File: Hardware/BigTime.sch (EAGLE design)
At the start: 13 parts, among them U1 ATMEGA328P_PDIP_EZ, Y1 32.768kHz

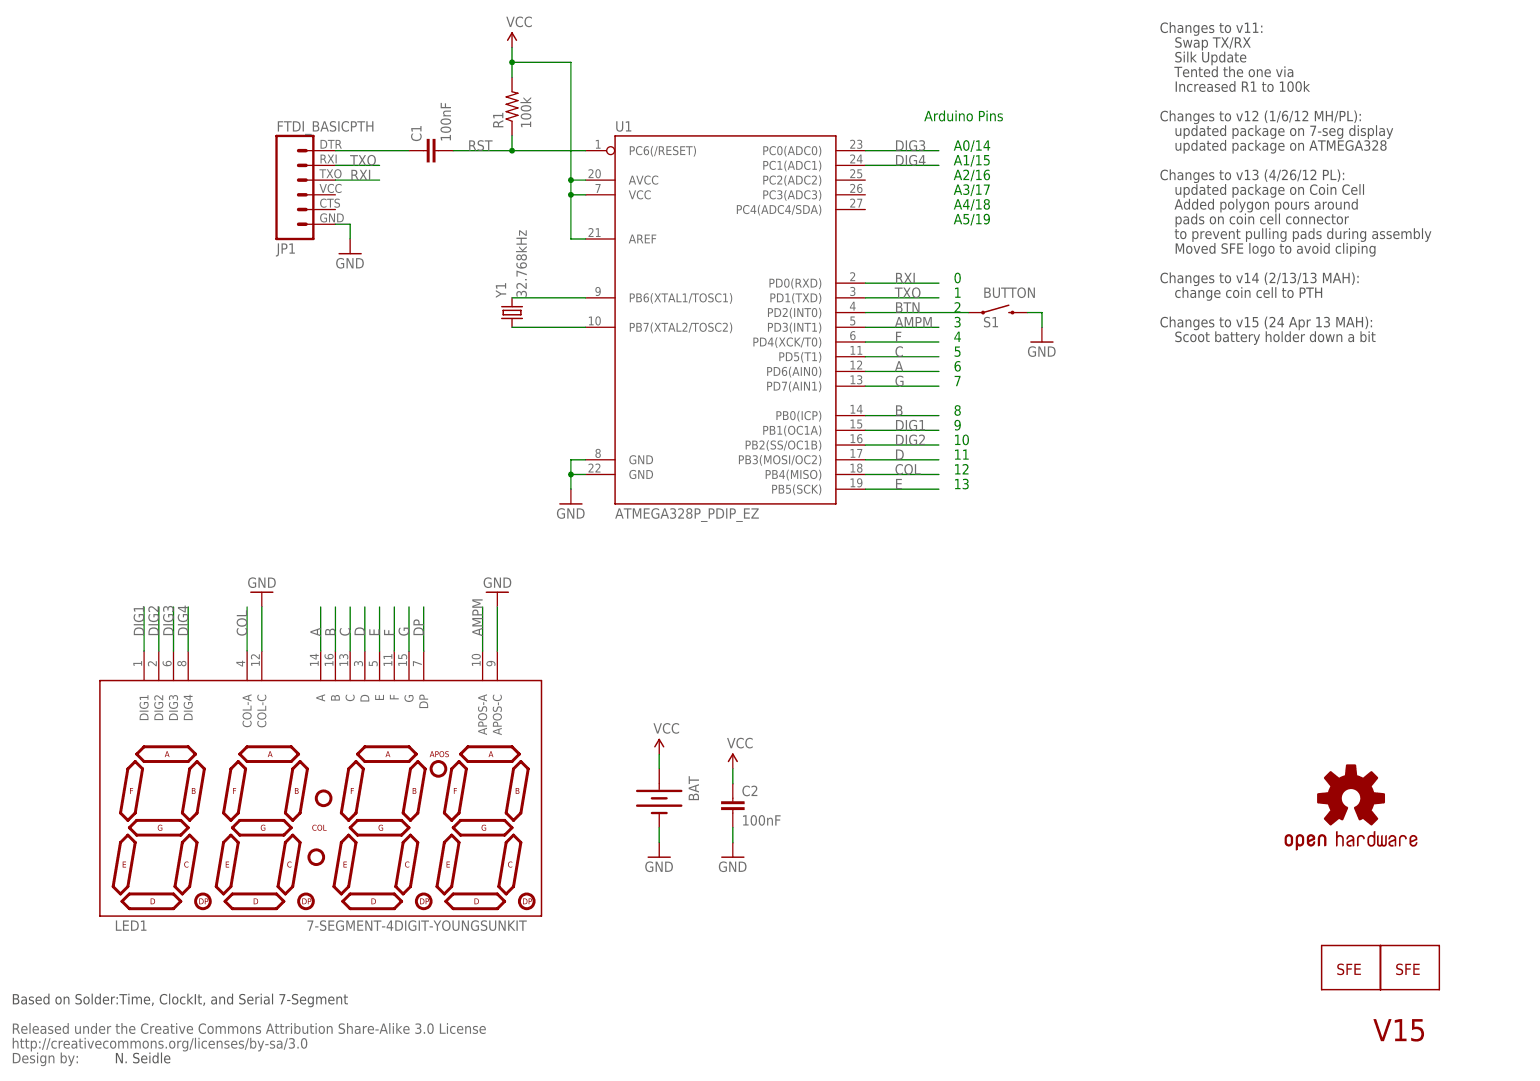
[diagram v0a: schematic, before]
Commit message: replace LED with bubble display
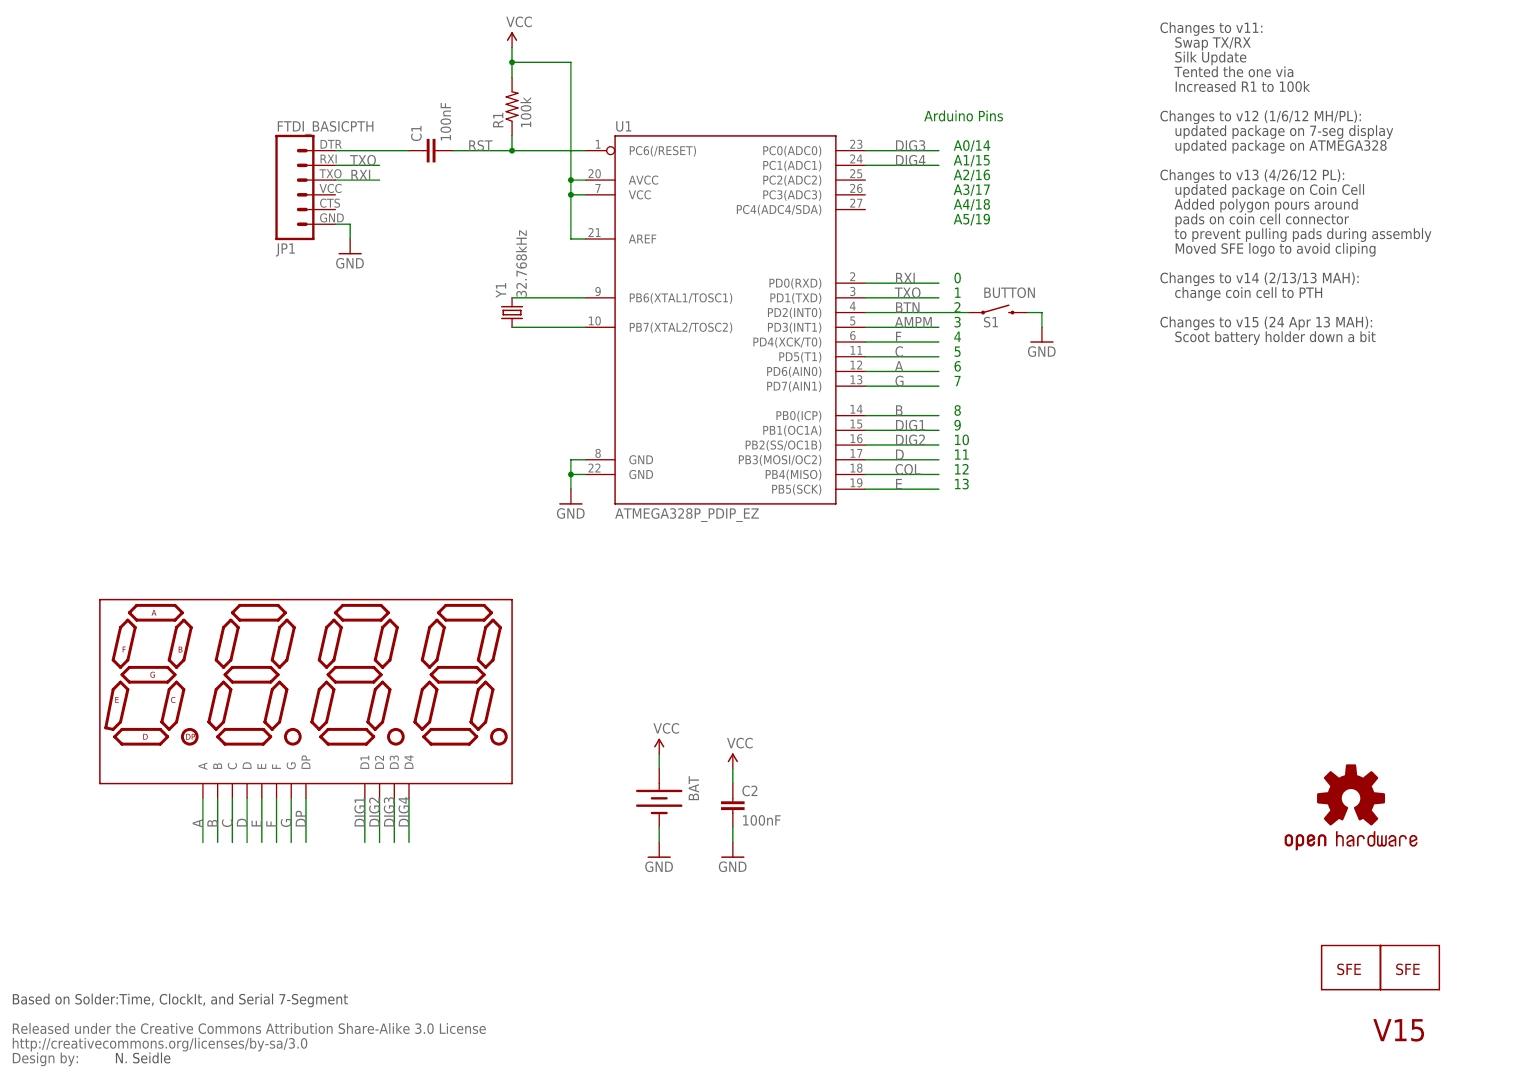
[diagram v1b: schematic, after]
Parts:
- removed LED1: 7-SEGMENT-4DIGIT-YOUNGSUNKIT, Testing:7-SEGMENT-4DIGIT-YOUNGSUNKIT
- added DISP1: 7-SEGMENT-4DIGIT-COUNTER-HP-BUBBLE, SparkFun-Displays:7-SEGMENT-4DIGIT-COUNTER-HP-BUBBLE
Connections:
- net A: now also DISP1.A; no longer LED1.A
- net AMPM: no longer LED1.APOS-A
- net B: now also DISP1.B; no longer LED1.B
- net C: now also DISP1.C; no longer LED1.C
- net COL: no longer LED1.COL-A
- net D: now also DISP1.D; no longer LED1.D
- net DIG1: now also DISP1.D1; no longer LED1.DIG1
- net DIG2: now also DISP1.D2; no longer LED1.DIG2
- net DIG3: now also DISP1.D3; no longer LED1.DIG3
- net DIG4: now also DISP1.D4; no longer LED1.DIG4
- net DP: now also DISP1.DP; no longer LED1.DP
- net E: now also DISP1.E; no longer LED1.E
- net F: now also DISP1.F; no longer LED1.F
- net G: now also DISP1.G; no longer LED1.G
- net GND: no longer LED1.APOS-C, LED1.COL-C

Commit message: add set button, reroute pub
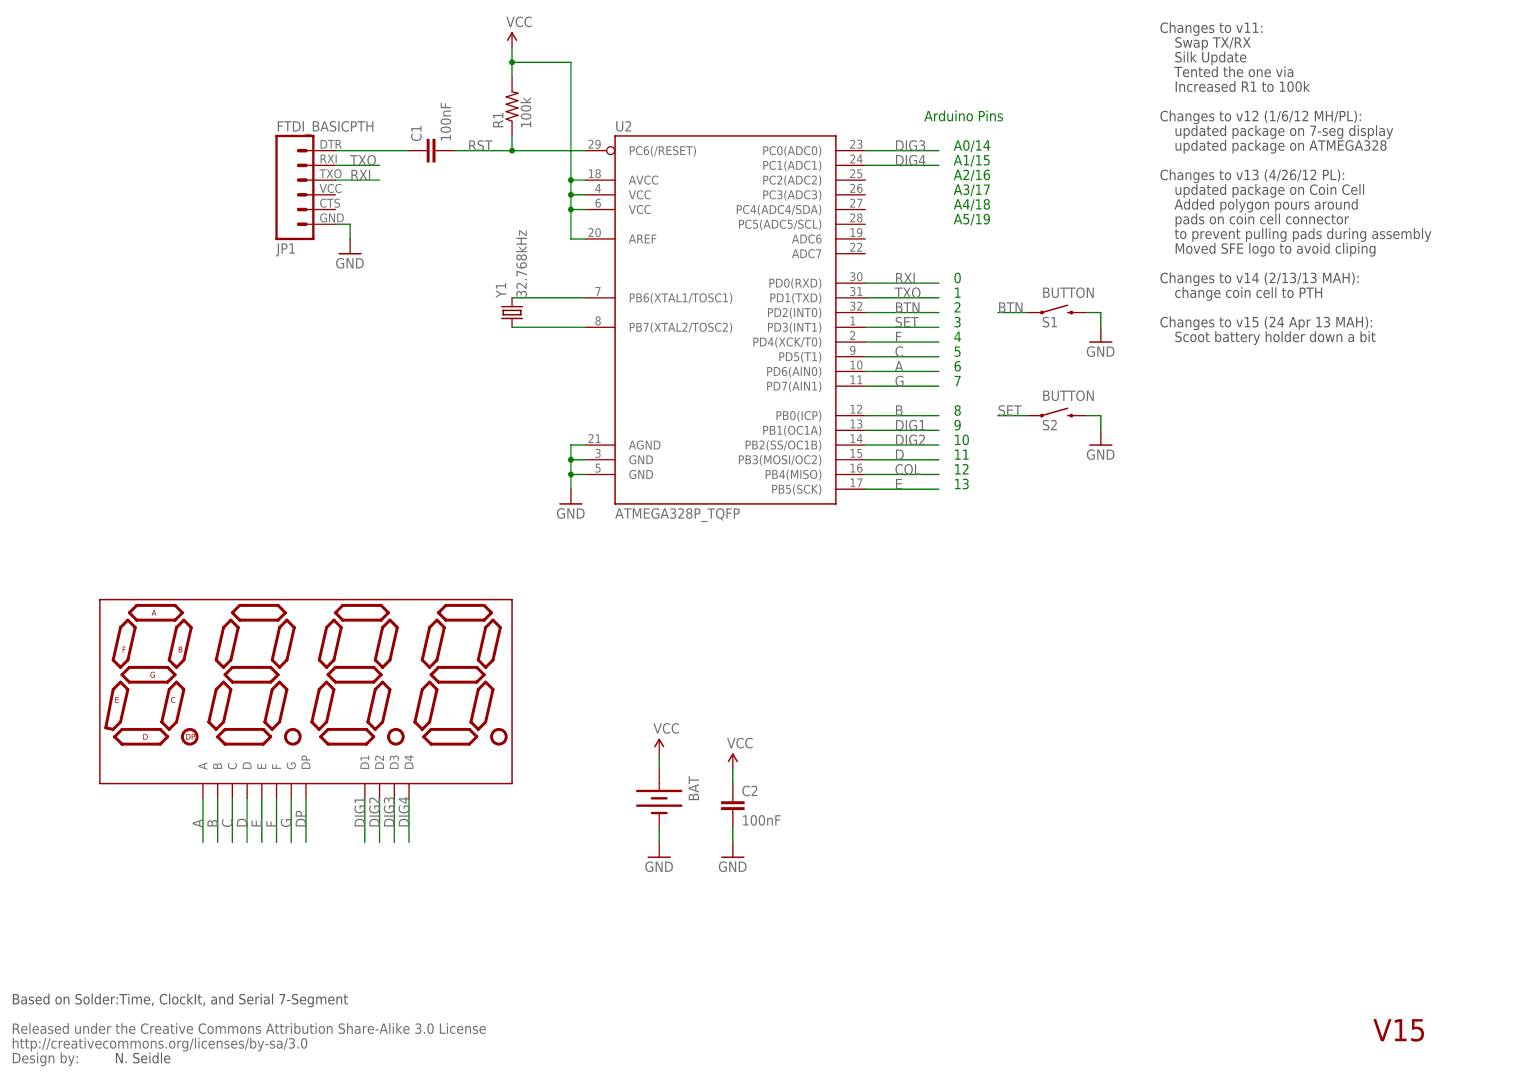
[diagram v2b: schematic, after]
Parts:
- removed U$1: LOGO-SFESK, SparkFun:LOGO-SFESK
- removed U$4: OSHW-LOGOS, SparkFun:OSHW-LOGOS
- removed U$5: LOGO-SFENW2, SparkFun:LOGO-SFENW2
- removed U1: ATMEGA328P_PDIP_EZ, SparkFun-DigitalIC:ATMEGA328P_PDIP_EZ
- added S2: BUTTON, SparkFun-Electromechanical:SWITCH-MOMENTARY-2SIDE_EZ
- added U2: ATMEGA328P_TQFP, SparkFun-DigitalIC:ATMEGA328P_TQFP
- C1, C2: device SparkFun-Passives:CAPEZ -> SparkFun-Passives:CAP0402-CAP
- DISP1: value 7-SEGMENT-4DIGIT-COUNTER-HP-BUBBLE -> 7-SEGMENT-4DIGIT-COUNTER-HP-BUBBLE-SM; device SparkFun-Displays:7-SEGMENT-4DIGIT-COUNTER-HP-BUBBLE -> SparkFun-Displays:7-SEGMENT-4DIGIT-COUNTER-HP-BUBBLE-SM
- R1: device SparkFun-Passives:RESISTORKIT -> SparkFun-Passives:RESISTOR0402-RES
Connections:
- removed net AMPM: U1.PD3(INT1)
- new net SET: S2.1, U2.PD3(INT1)
- net A: now also U2.PD6(AIN0); no longer U1.PD6(AIN0)
- net B: now also U2.PB0(ICP); no longer U1.PB0(ICP)
- net BTN: now also U2.PD2(INT0); no longer U1.PD2(INT0)
- net C: now also U2.PD5(T1); no longer U1.PD5(T1)
- net COL: now also U2.PB4(MISO); no longer U1.PB4(MISO)
- net D: now also U2.PB3(MOSI/OC2); no longer U1.PB3(MOSI/OC2)
- net DIG1: now also U2.PB1(OC1A); no longer U1.PB1(OC1A)
- net DIG2: now also U2.PB2(SS/OC1B); no longer U1.PB2(SS/OC1B)
- net DIG3: now also U2.PC0(ADC0); no longer U1.PC0(ADC0)
- net DIG4: now also U2.PC1(ADC1); no longer U1.PC1(ADC1)
- net E: now also U2.PB5(SCK); no longer U1.PB5(SCK)
- net F: now also U2.PD4(XCK/T0); no longer U1.PD4(XCK/T0)
- net G: now also U2.PD7(AIN1); no longer U1.PD7(AIN1)
- net GND: now also S2.2, U2.AGND, U2.GND@3, U2.GND@5; no longer U1.GND@1, U1.GND@2
- net N$1: now also U2.PB7(XTAL2/TOSC2); no longer U1.PB7(XTAL2/TOSC2)
- net N$2: now also U2.PB6(XTAL1/TOSC1); no longer U1.PB6(XTAL1/TOSC1)
- net RST: now also U2.PC6(/RESET); no longer U1.PC6(/RESET)
- net RXI: now also U2.PD0(RXD); no longer U1.PD0(RXD)
- net TXO: now also U2.PD1(TXD); no longer U1.PD1(TXD)
- net VCC: now also U2.AREF, U2.AVCC, U2.VCC@4, U2.VCC@6; no longer U1.AREF, U1.AVCC, U1.VCC
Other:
- moved on the sheet: S1

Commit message: more efficient pin arrangement
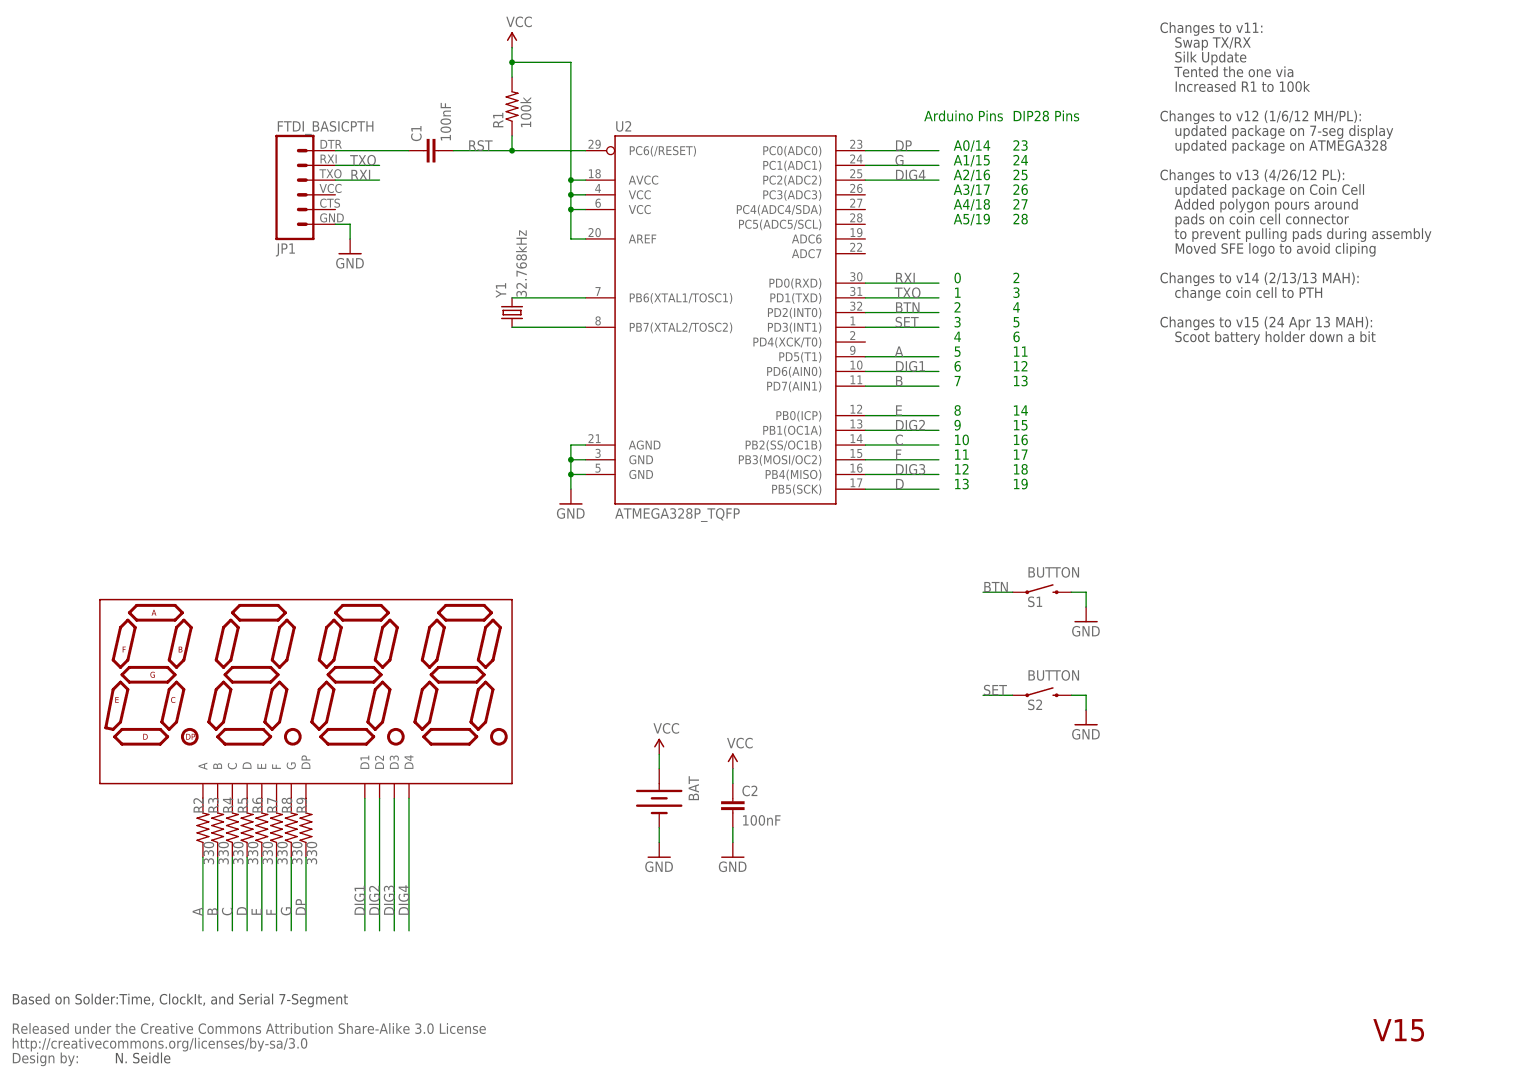
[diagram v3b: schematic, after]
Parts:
- added R2, R3, R4, R5, R6, R7, R8, R9: 330, SparkFun-Passives:RESISTOR0402-RES
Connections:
- removed net COL: U2.PB4(MISO)
- new net N$10: DISP1.G, R8.2
- new net N$11: DISP1.DP, R9.2
- new net N$4: DISP1.A, R2.2
- new net N$5: DISP1.B, R3.2
- new net N$6: DISP1.C, R4.2
- new net N$7: DISP1.D, R5.2
- new net N$8: DISP1.E, R6.2
- new net N$9: DISP1.F, R7.2
- net A: now also R2.1, U2.PD5(T1); no longer DISP1.A, U2.PD6(AIN0)
- net B: now also R3.1, U2.PD7(AIN1); no longer DISP1.B, U2.PB0(ICP)
- net C: now also R4.1, U2.PB2(SS/OC1B); no longer DISP1.C, U2.PD5(T1)
- net D: now also R5.1, U2.PB5(SCK); no longer DISP1.D, U2.PB3(MOSI/OC2)
- net DIG1: now also U2.PD6(AIN0); no longer U2.PB1(OC1A)
- net DIG2: now also U2.PB1(OC1A); no longer U2.PB2(SS/OC1B)
- net DIG3: now also U2.PB4(MISO); no longer U2.PC0(ADC0)
- net DIG4: no longer U2.PC1(ADC1)
- net DP: now also R9.1, U2.PC0(ADC0); no longer DISP1.DP
- net E: now also R6.1, U2.PB0(ICP); no longer DISP1.E, U2.PB5(SCK)
- net F: now also R7.1, U2.PB3(MOSI/OC2); no longer DISP1.F, U2.PD4(XCK/T0)
- net G: now also R8.1, U2.PC1(ADC1); no longer DISP1.G, U2.PD7(AIN1)
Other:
- note added: "14"
- note added: "15"
- note added: "16"
- note added: "17"
- note added: "18"
- note added: "19"
- note added: "23"
- note added: "24"
- note added: "25"
- note added: "26"
- note added: "27"
- note added: "28"
- note added: "DIP28 Pins"
- moved on the sheet: S1, S2

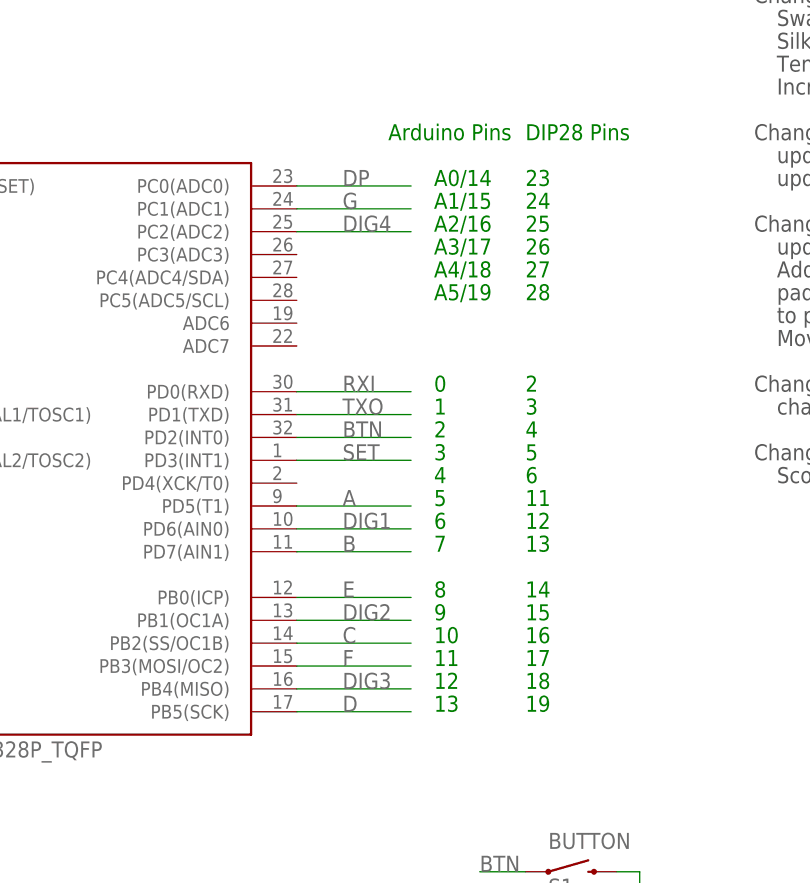
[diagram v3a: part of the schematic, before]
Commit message: rearrange pins, start fitting to size
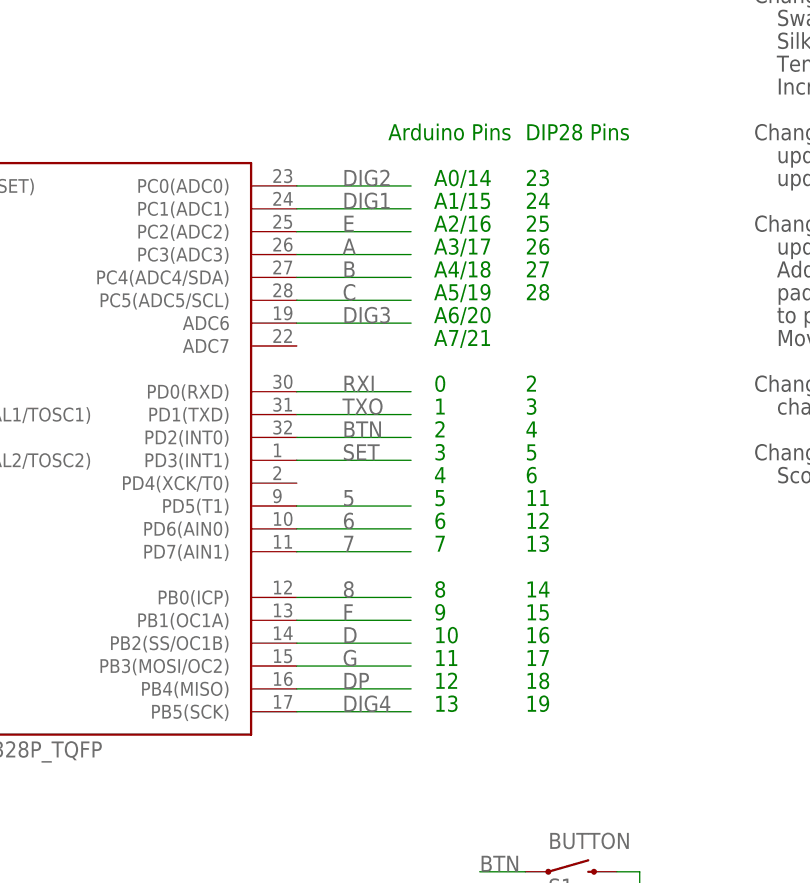
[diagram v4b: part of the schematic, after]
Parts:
- Y1: device SparkFun-FreqCtrl:CRYSTALTC26H_EZ -> SparkFun-FreqCtrl:CRYSTAL32-SMD
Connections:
- new net 5: U2.PD5(T1)
- new net 6: U2.PD6(AIN0)
- new net 7: U2.PD7(AIN1)
- new net 8: U2.PB0(ICP)
- net A: now also U2.PC3(ADC3); no longer U2.PD5(T1)
- net B: now also U2.PC4(ADC4/SDA); no longer U2.PD7(AIN1)
- net C: now also U2.PC5(ADC5/SCL); no longer U2.PB2(SS/OC1B)
- net D: now also U2.PB2(SS/OC1B); no longer U2.PB5(SCK)
- net DIG1: now also U2.PC1(ADC1); no longer U2.PD6(AIN0)
- net DIG2: now also U2.PC0(ADC0); no longer U2.PB1(OC1A)
- net DIG3: now also U2.ADC6; no longer U2.PB4(MISO)
- net DIG4: now also U2.PB5(SCK)
- net DP: now also U2.PB4(MISO); no longer U2.PC0(ADC0)
- net E: now also U2.PC2(ADC2); no longer U2.PB0(ICP)
- net F: now also U2.PB1(OC1A); no longer U2.PB3(MOSI/OC2)
- net G: now also U2.PB3(MOSI/OC2); no longer U2.PC1(ADC1)
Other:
- note added: "A6/20"
- note added: "A7/21"
